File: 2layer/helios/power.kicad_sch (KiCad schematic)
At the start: 3 parts, among them J1 Conn_01x03

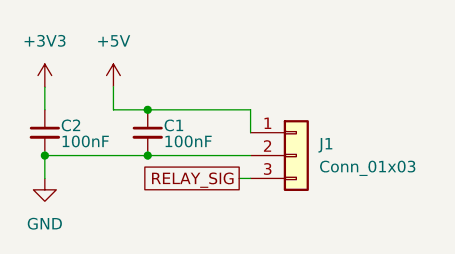
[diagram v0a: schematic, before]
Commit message: added MCU code + documentation
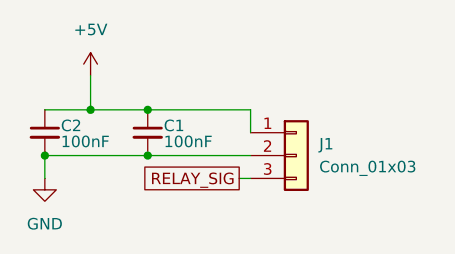
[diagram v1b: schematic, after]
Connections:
- net +3V3 is gone; now on net +5V: C2.1
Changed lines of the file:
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@@
 	(title_block
 		(title "Power Module")
-		(date "2026-07-01")
-		(rev "1.0")
+		(date "2026-07-17")
+		(rev "1.2")
 		(company "Purit (Kin) Hongjirakul")
 		(comment 1 "Real-Time Lamp Controller")
@@
 	)
 	(junction
+		(at 139.7 97.79)
+		(diameter 0)
+		(color 0 0 0 0)
+	)
+	(junction
+		(at 133.35 97.79)
+		(diameter 0)
+		(color 0 0 0 0)
+	)
+	(junction
 		(at 128.27 102.87)
 		(diameter 0)
 		(color 0 0 0 0)
 	)
-	(junction
-		(at 139.7 97.79)
-		(diameter 0)
-		(color 0 0 0 0)
-	)
-	(wire
-		(pts
-			(xy 135.89 97.79) (xy 139.7 97.79)
-		)
-		(stroke
-			(width 0)
-			(type default)
-		)
-	)
-	(wire
-		(pts
-			(xy 128.27 95.25) (xy 128.27 97.79)
+	(wire
+		(pts
+			(xy 128.27 97.79) (xy 133.35 97.79)
 		)
 		(stroke
@@
 	(wire
 		(pts
+			(xy 133.35 93.98) (xy 133.35 97.79)
+		)
+		(stroke
+			(width 0)
+			(type default)
+		)
+	)
+	(wire
+		(pts
 			(xy 149.86 105.41) (xy 151.13 105.41)
 		)
@@
 	(wire
 		(pts
-			(xy 135.89 95.25) (xy 135.89 97.79)
+			(xy 133.35 97.79) (xy 139.7 97.79)
 		)
 		(stroke
@@
 		)
 		(instances
-			(project "rtlc"
+			(project "helios"
 				(path "/420197ff-90a6-4457-b334-95b83749cbd4/27c51c78-1ca5-45fa-a476-50b2346ca4b0"
 					(reference "C2")
@@
 		)
 		(instances
-			(project "rtlc"
+			(project "helios"
 				(path "/420197ff-90a6-4457-b334-95b83749cbd4/27c51c78-1ca5-45fa-a476-50b2346ca4b0"
 					(reference "#PWR05")
@@
 	)
 	(symbol
-		(lib_id "power:+3V3")
-		(at 128.27 95.25 0)
-		(unit 1)
-		(body_style 1)
-		(exclude_from_sim no)
-		(in_bom yes)
-		(on_board yes)
-		(in_pos_files yes)
-		(dnp no)
-		(fields_autoplaced yes)
-		(property "Reference" "#PWR07"
-			(at 128.27 99.06 0)
-			(hide yes)
-			(show_name no)
-			(do_not_autoplace no)
-			(effects
-				(font
-					(size 1.27 1.27)
-				)
-			)
-		)
-		(property "Value" "+3V3"
-			(at 128.27 90.17 0)
-			(show_name no)
-			(do_not_autoplace no)
-			(effects
-				(font
-					(size 1.27 1.27)
-				)
-			)
-		)
-		(property "Footprint" ""
-			(at 128.27 95.25 0)
-			(hide yes)
-			(show_name no)
-			(do_not_autoplace no)
-			(effects
-				(font
-					(size 1.27 1.27)
-				)
-			)
-		)
-		(property "Datasheet" ""
-			(at 128.27 95.25 0)
-			(hide yes)
-			(show_name no)
-			(do_not_autoplace no)
-			(effects
-				(font
-					(size 1.27 1.27)
-				)
-			)
-		)
-		(property "Description" "Power symbol creates a global label with name \"+3V3\""
-			(at 128.27 95.25 0)
-			(hide yes)
-			(show_name no)
-			(do_not_autoplace no)
-			(effects
-				(font
-					(size 1.27 1.27)
-				)
-			)
-		)
-		(pin "1"
-		)
-		(instances
-			(project "rtlc"
-				(path "/420197ff-90a6-4457-b334-95b83749cbd4/27c51c78-1ca5-45fa-a476-50b2346ca4b0"
-					(reference "#PWR07")
-					(unit 1)
-				)
-			)
-		)
-	)
-	(symbol
 		(lib_id "power:+5V")
-		(at 135.89 95.25 0)
+		(at 133.35 93.98 0)
 		(unit 1)
 		(body_style 1)
@@
 		(fields_autoplaced yes)
 		(property "Reference" "#PWR06"
-			(at 135.89 99.06 0)
+			(at 133.35 97.79 0)
 			(hide yes)
 			(show_name no)
@@
 		)
 		(property "Value" "+5V"
-			(at 135.89 90.17 0)
+			(at 133.35 88.9 0)
 			(show_name no)
 			(do_not_autoplace no)
@@
 		)
 		(property "Footprint" ""
-			(at 135.89 95.25 0)
+			(at 133.35 93.98 0)
 			(hide yes)
 			(show_name no)
@@
 		)
 		(property "Datasheet" ""
-			(at 135.89 95.25 0)
+			(at 133.35 93.98 0)
 			(hide yes)
 			(show_name no)
@@
 		)
 		(property "Description" "Power symbol creates a global label with name \"+5V\""
-			(at 135.89 95.25 0)
+			(at 133.35 93.98 0)
 			(hide yes)
 			(show_name no)
@@
 		)
 		(instances
-			(project "rtlc"
+			(project "helios"
 				(path "/420197ff-90a6-4457-b334-95b83749cbd4/27c51c78-1ca5-45fa-a476-50b2346ca4b0"
 					(reference "#PWR06")
@@
 		)
 		(instances
-			(project "rtlc"
+			(project "helios"
 				(path "/420197ff-90a6-4457-b334-95b83749cbd4/27c51c78-1ca5-45fa-a476-50b2346ca4b0"
 					(reference "J1")
@@
 		)
 		(instances
-			(project "rtlc"
+			(project "helios"
 				(path "/420197ff-90a6-4457-b334-95b83749cbd4/27c51c78-1ca5-45fa-a476-50b2346ca4b0"
 					(reference "C1")
